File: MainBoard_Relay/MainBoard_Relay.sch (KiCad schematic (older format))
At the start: 11 parts, among them J1 Conn_01x03_Female, J2 Conn_01x03_Female, K1 G5Q-1, K2 RAC01-05SGB, Q1 Q_NMOS_DGS, U1 ESP-01v090, U2 AZ1117-3.3

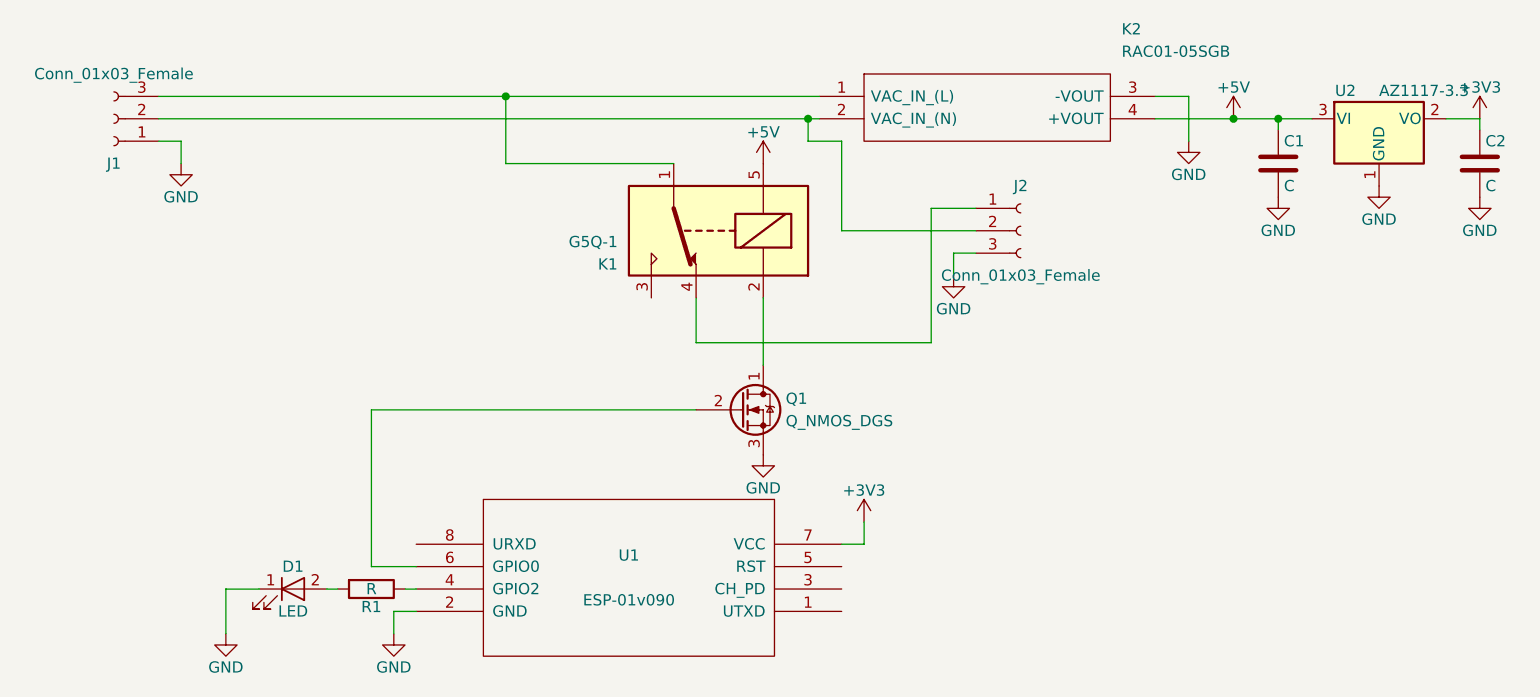
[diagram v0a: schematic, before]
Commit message: RGB and Relay platform finished
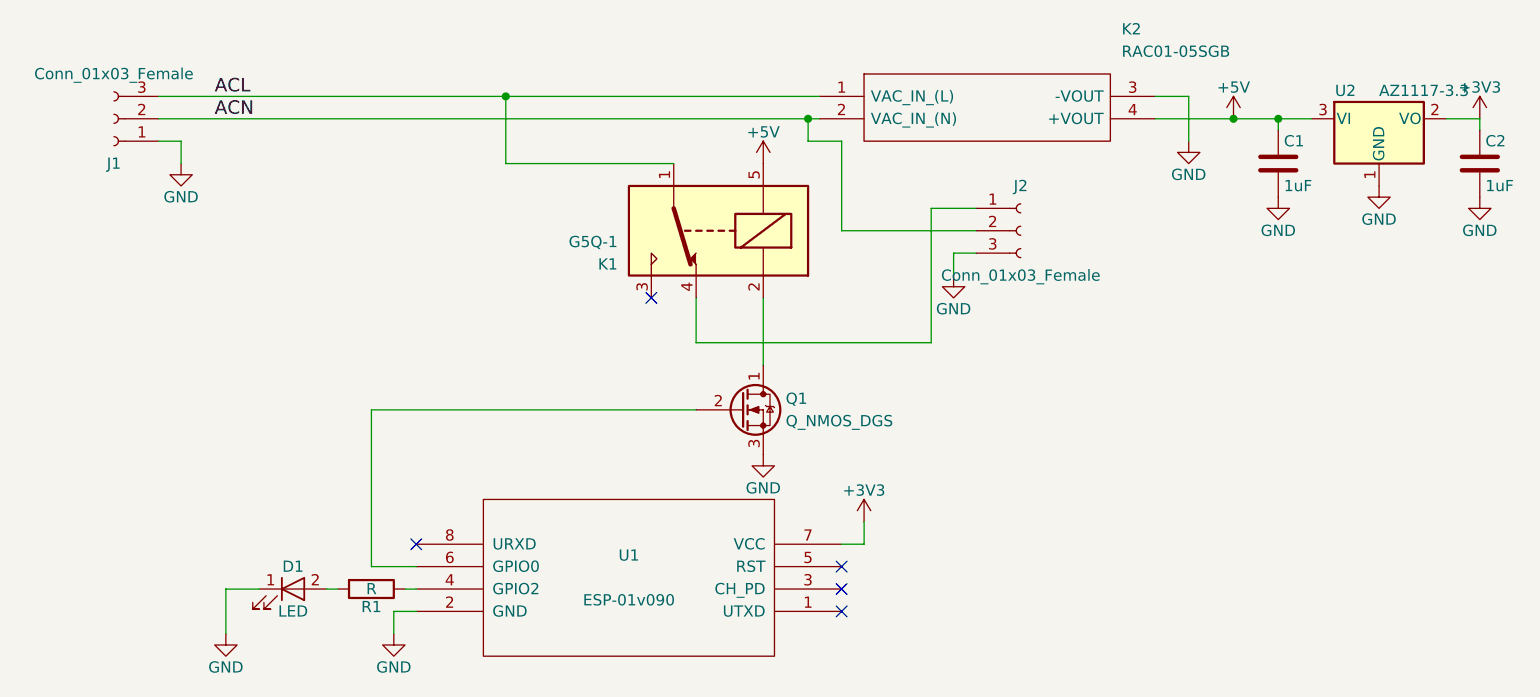
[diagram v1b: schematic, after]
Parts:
- C1, C2: value C -> 1uF
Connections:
- net ACL: now reaches J1.3 (Pin_3), K1.1, K2.1 (VAC_IN_(L))
- net ACN: now reaches J1.2 (Pin_2), J2.2 (Pin_2), K2.2 (VAC_IN_(N))
- no-connect marks 0 -> 5
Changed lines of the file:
@@
 LIBS:contrib
 LIBS:valves
-LIBS:ESP8266
-LIBS:RAC01-05SGB
+LIBS:MainBoard_Relay-cache
 EELAYER 25 0
 EELAYER END
@@
 P 8850 1250
 F 0 "C1" H 8875 1350 50  0000 L CNN
-F 1 "C" H 8875 1150 50  0000 L CNN
+F 1 "1uF" H 8875 1150 50  0000 L CNN
 F 2 "Capacitors_SMD:C_0805_HandSoldering" H 8888 1100 50  0001 C CNN
 F 3 "" H 8850 1250 50  0001 C CNN
@@
 P 9750 1250
 F 0 "C2" H 9775 1350 50  0000 L CNN
-F 1 "C" H 9775 1150 50  0000 L CNN
+F 1 "1uF" H 9775 1150 50  0000 L CNN
 F 2 "Capacitors_SMD:C_0805_HandSoldering" H 9788 1100 50  0001 C CNN
 F 3 "" H 9750 1250 50  0001 C CNN
@@
 Wire Wire Line
 	4650 3150 4600 3150
+NoConn ~ 5000 2950
+NoConn ~ 6900 3050
+NoConn ~ 6900 3150
+NoConn ~ 6900 3250
+NoConn ~ 6050 1850
+Text Label 4100 1050 0    60   ~ 0
+ACN
+Text Label 4100 950  0    60   ~ 0
+ACL
 $EndSCHEMATC
